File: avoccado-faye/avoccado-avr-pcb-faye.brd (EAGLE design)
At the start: 25 x 24.5 mm, 61 parts, among them Q1 16MHz, Q2 FET, U2 MCP73831

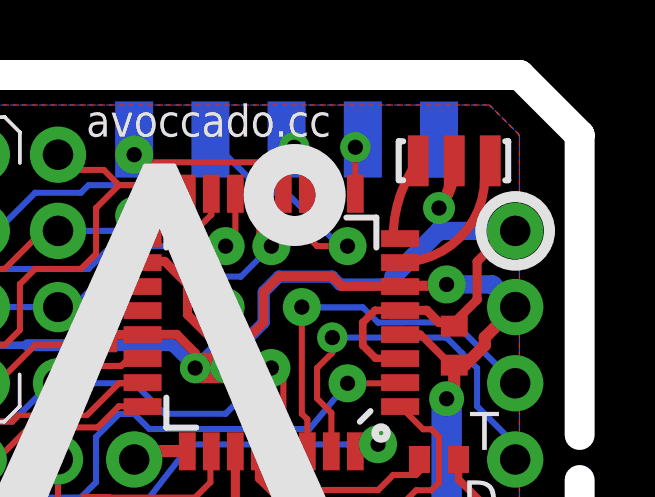
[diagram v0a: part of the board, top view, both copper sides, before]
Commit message: spacing of resonator slightly larger
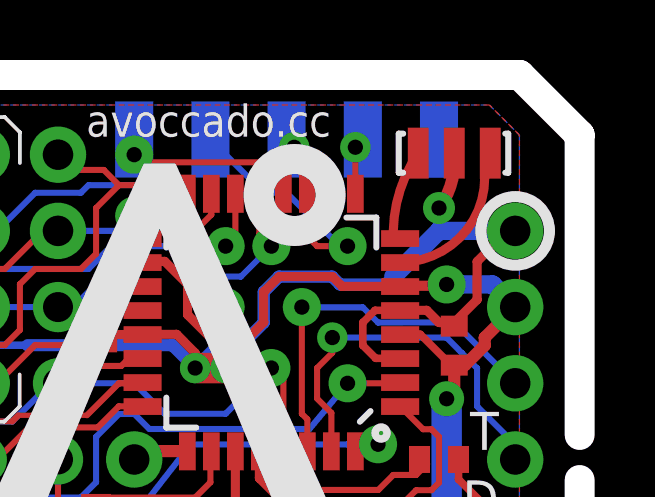
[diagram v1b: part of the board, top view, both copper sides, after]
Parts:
- moved Q1 0.25 mm to (20.3, 21.4)
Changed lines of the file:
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@@
 <setting verticaltext="up"/>
 </settings>
-<grid distance="1" unitdist="mm" unit="mm" style="lines" multiple="1" display="yes" altdistance="0.1" altunitdist="mm" altunit="mm"/>
+<grid distance="0.02" unitdist="inch" unit="inch" style="lines" multiple="1" display="yes" altdistance="0.01" altunitdist="inch" altunit="inch"/>
 <layers>
 <layer number="1" name="Top" color="47" fill="1" visible="yes" active="yes"/>
@@
 <layer number="14" name="Route14" color="1" fill="6" visible="no" active="no"/>
 <layer number="15" name="Route15" color="4" fill="6" visible="no" active="no"/>
-<layer number="16" name="Bottom" color="39" fill="1" visible="no" active="yes"/>
+<layer number="16" name="Bottom" color="39" fill="1" visible="yes" active="yes"/>
 <layer number="17" name="Pads" color="14" fill="1" visible="yes" active="yes"/>
 <layer number="18" name="Vias" color="6" fill="1" visible="yes" active="yes"/>
@@
 <layer number="20" name="Dimension" color="15" fill="1" visible="yes" active="yes"/>
 <layer number="21" name="tPlace" color="15" fill="1" visible="yes" active="yes"/>
-<layer number="22" name="bPlace" color="6" fill="1" visible="no" active="yes"/>
+<layer number="22" name="bPlace" color="6" fill="1" visible="yes" active="yes"/>
 <layer number="23" name="tOrigins" color="15" fill="1" visible="yes" active="yes"/>
-<layer number="24" name="bOrigins" color="15" fill="1" visible="no" active="yes"/>
+<layer number="24" name="bOrigins" color="15" fill="1" visible="yes" active="yes"/>
 <layer number="25" name="tNames" color="7" fill="1" visible="yes" active="yes"/>
-<layer number="26" name="bNames" color="7" fill="1" visible="no" active="yes"/>
+<layer number="26" name="bNames" color="7" fill="1" visible="yes" active="yes"/>
 <layer number="27" name="tValues" color="7" fill="1" visible="yes" active="yes"/>
-<layer number="28" name="bValues" color="7" fill="1" visible="no" active="yes"/>
+<layer number="28" name="bValues" color="7" fill="1" visible="yes" active="yes"/>
 <layer number="29" name="tStop" color="7" fill="3" visible="yes" active="yes"/>
 <layer number="30" name="bStop" color="7" fill="6" visible="yes" active="yes"/>
@@
 <wire x1="24.5" y1="12" x2="24.5" y2="22" width="1" layer="46"/>
 <wire x1="24.5" y1="22" x2="22.5" y2="24" width="1" layer="46"/>
-<rectangle x1="10.668" y1="11.684" x2="18.796" y2="19.812" layer="41"/>
+<rectangle x1="10.16" y1="11.684" x2="18.288" y2="19.812" layer="41"/>
 <circle x="22.352" y="1.024" radius="1.143" width="0.3683" layer="22"/>
 <circle x="9.652" y="1.024" radius="1.143" width="0.3683" layer="22"/>
@@
 <element name="C3" library="SparkFun" package="C0402" value="0.1uF" x="20.32" y="14.978" smashed="yes" rot="R270"/>
 <element name="C1" library="SparkFun" package="C0402" value="0.1uF" x="8.636" y="15.756" smashed="yes" rot="R90"/>
-<element name="Q1" library="SparkFun" package="RESONATOR-SMD" value="16MHz" x="20.32" y="21.1408" smashed="yes">
-<attribute name="VALUE" x="18.26905625" y="19.52258125" size="0.6096" layer="27" ratio="15"/>
+<element name="Q1" library="SparkFun" package="RESONATOR-SMD" value="16MHz" x="20.32" y="21.3948" smashed="yes">
+<attribute name="VALUE" x="18.26905625" y="19.77658125" size="0.6096" layer="27" ratio="15"/>
 </element>
 <element name="Q2" library="SparkFun-DiscreteSemi" package="SOT23-3" value="FET" x="2.032" y="2.286" smashed="yes" rot="R270">
@@
 <wire x1="11.684" y1="14.232" x2="11.684" y2="14.732" width="0.3048" layer="1"/>
 <wire x1="11.684" y1="14.732" x2="11.068" y2="15.356" width="0.3048" layer="1"/>
-<wire x1="20.32" y1="21.1408" x2="20.32" y2="21.09" width="0.4064" layer="1"/>
+<wire x1="20.32" y1="21.3948" x2="20.32" y2="21.09" width="0.4064" layer="1"/>
 <wire x1="20.32" y1="21.09" x2="19.812" y2="19.566" width="0.4064" layer="1" curve="-36.869898"/>
 <contactref element="JP4" pad="2"/>
@@
 <contactref element="Q1" pad="1"/>
 <wire x1="18.288" y1="18.7846" x2="18.288" y2="18.804" width="0.254" layer="1"/>
-<wire x1="18.288" y1="18.804" x2="19.12" y2="21.1408" width="0.3048" layer="1" curve="-33.165053"/>
+<wire x1="18.288" y1="18.804" x2="19.12" y2="21.3948" width="0.3048" layer="1" curve="-33.165053"/>
 <contactref element="MCU" pad="8"/>
 <wire x1="18.5166" y1="18.548" x2="18.288" y2="18.7846" width="0" layer="19" extent="1-1"/>
@@
 <wire x1="21.336" y1="20.5754" x2="21.336" y2="20.836" width="0.3048" layer="1"/>
 <wire x1="21.336" y1="20.836" x2="21.52" y2="21.02" width="0.254" layer="1" curve="90"/>
-<wire x1="21.52" y1="21.02" x2="21.52" y2="21.1408" width="0.254" layer="1"/>
+<wire x1="21.52" y1="21.02" x2="21.52" y2="21.3948" width="0.254" layer="1"/>
 <contactref element="MCU" pad="7"/>
 <wire x1="18.5166" y1="17.748" x2="18.5166" y2="17.756" width="0" layer="19" extent="1-1"/>

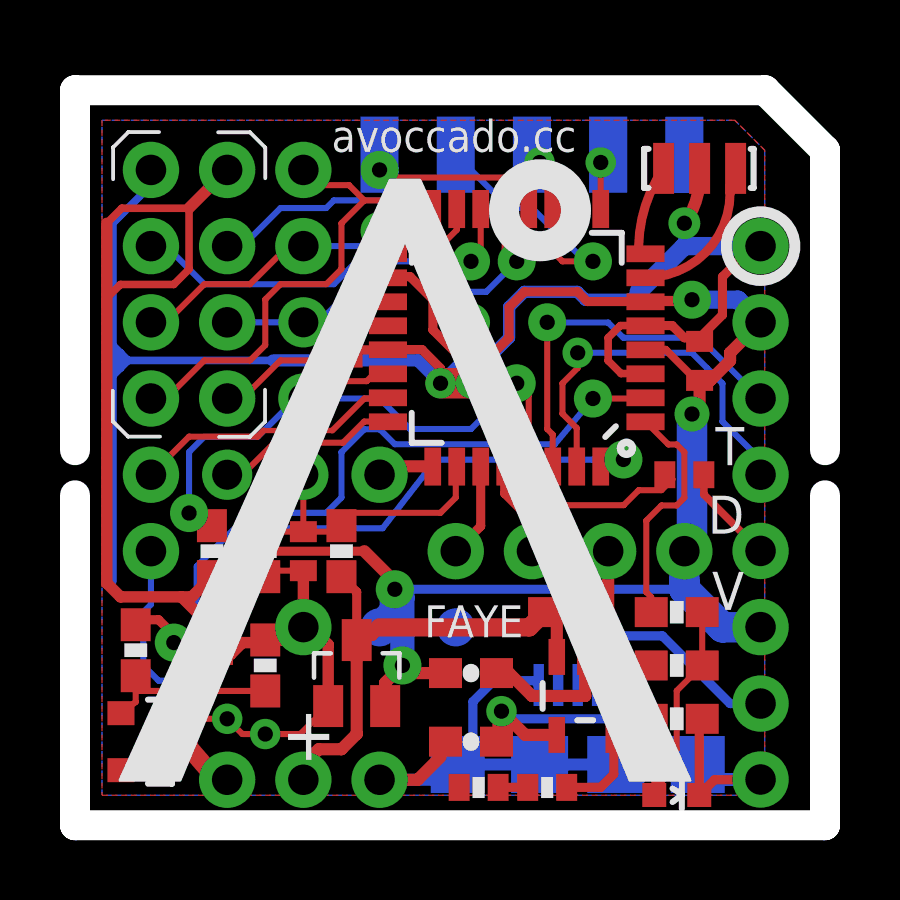
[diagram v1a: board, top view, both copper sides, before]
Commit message: milling paths ready for matrix panelizing
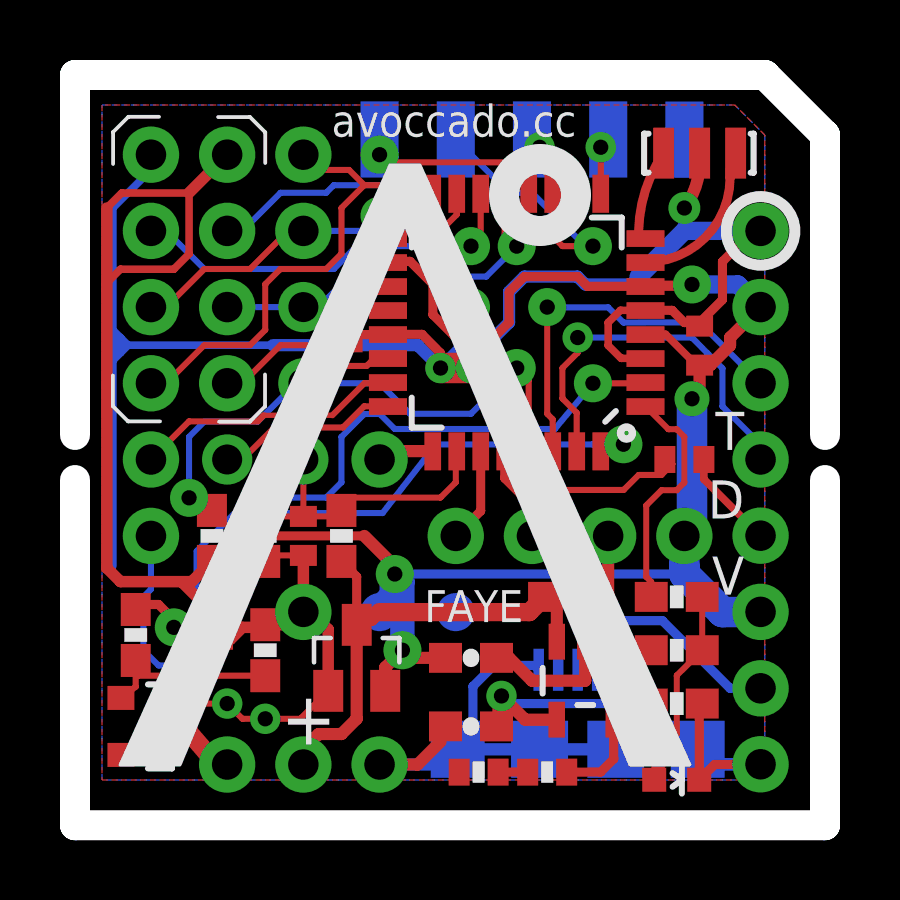
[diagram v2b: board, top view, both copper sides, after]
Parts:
- moved JP13 0.51 mm to (7.11, 19.3)
- moved JP27 0.51 mm to (2.03, 19.3)
- moved JP3 0.51 mm to (22.4, 19.3)
- moved C2 0.51 mm to (19.8, 11.7)
- moved C3 0.51 mm to (20.3, 15.5)
- moved C7 0.51 mm to (7.11, 9.14)
- moved JP19 0.51 mm to (2.03, 11.7)
- moved JP20 0.51 mm to (4.57, 11.7)
- moved JP21 0.51 mm to (9.65, 11.7)
- moved JP22 0.51 mm to (7.11, 11.7)
- moved JP4 0.51 mm to (19.8, 9.14)
- moved JP5 0.51 mm to (14.7, 9.14)
- moved JP9 0.51 mm to (22.4, 11.7)
- moved MCU 0.51 mm to (14.2, 16.3)
- moved R2 0.51 mm to (4.06, 9.14)
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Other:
- board size 25 x 24.5 mm -> 25 x 25 mm
